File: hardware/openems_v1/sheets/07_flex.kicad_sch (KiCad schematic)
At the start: 0 parts

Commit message: feat(hw): fecha esquemático v2 — sheets 01/02/03/05/07/11 desenhadas, ERC 0
- 01_power: nova — P-FET reverse (Q1) + F1 30A + SMBJ24CA + bulk 100µF/100nF,
  star GND (PGND/SGND/AGND) via PWR_FLAG na sheet produtora, VBAT limpo para
  o resto da placa (buck/LDO ficam no TPS65381A, sheet PMIC)
- 02_ckp / 03_cmp: CKP Hall (espelho do CMP) → MCU.PA0/PA1
- 05_analog: refeita do zero a partir do pinout_v2 (13 canais ADC), mapa
  pré-v2 descartado
- 11_mcu_h562: netlist U1 corrigido (lib_id não resolvia pinos — 100 pinos
  caíam na mesma net); globals PA0/PA1/PB4 sincronizados com as sheets acima
- 07_flex: pino corrigido para PB4 (pinout_v2)
- READMEs (hardware/openems_v1, docs/hw/schematic) actualizados ao estado
  real por sheet

Passos 1-5 do roadmap do esquemático fechados; ERC isolado por sheet em 0
erros (avisos residuais são globals sem sheet destino ainda — esperado).

Co-Authored-By: Claude Sonnet 5 <noreply@anthropic.com>
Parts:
- added D1: 3V3 unidirectional, Diode_SMD:D_SOD-123, symbol Device:D_TVS
- added R1, R3: 10k, Resistor_SMD:R_0603_1608Metric, symbol Device:R
- added R2: 3k3, Resistor_SMD:R_0603_1608Metric, symbol Device:R
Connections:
- new net +5V_SENS_B: R3.1
- new net AGND: D1.2 (A2)
- new net J1.FLEX_SIG: R1.1
- new net MCU.PB4: D1.1 (A1), R1.2, R2.1, R3.2
- new net SGND: R2.2

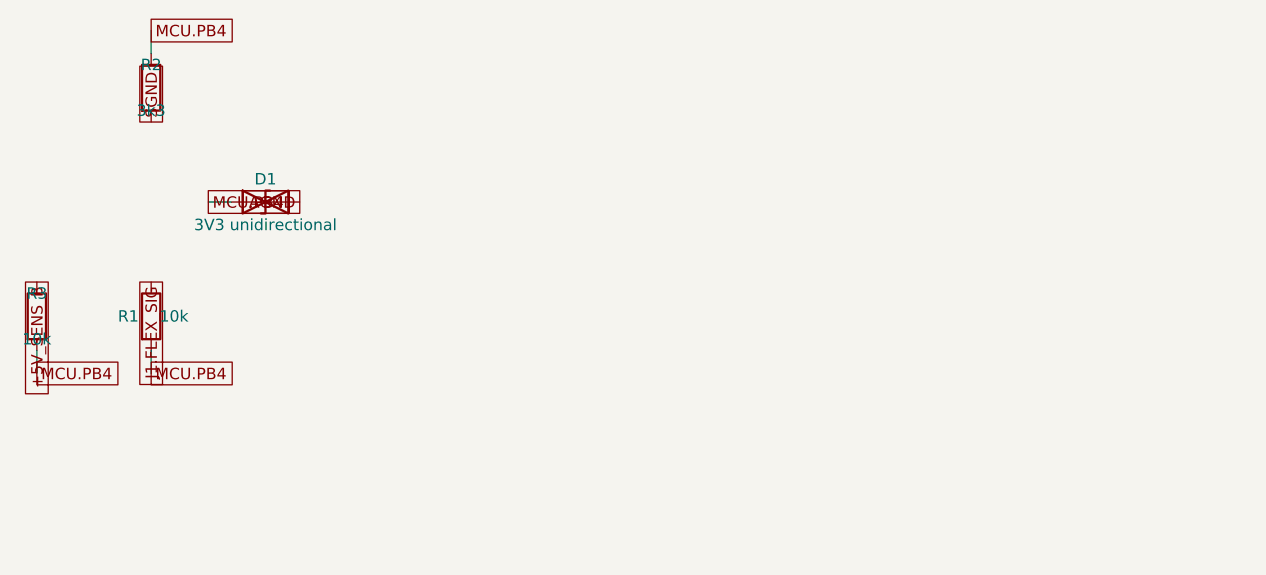
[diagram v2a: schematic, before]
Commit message: fix(hw): corrige legibilidade de 03_cmp e 07_flex — mesmo tratamento
03_cmp era clone directo do 02_ckp pré-correção (mesmo pitch de 12.7mm,
mesma sobreposição). 07_flex tinha o mesmo padrão em menor escala.
Reconstruídas com o layout validado no commit anterior — conectividade
idêntica, ERC 0 erros nas duas.

Co-Authored-By: Claude Sonnet 5 <noreply@anthropic.com>
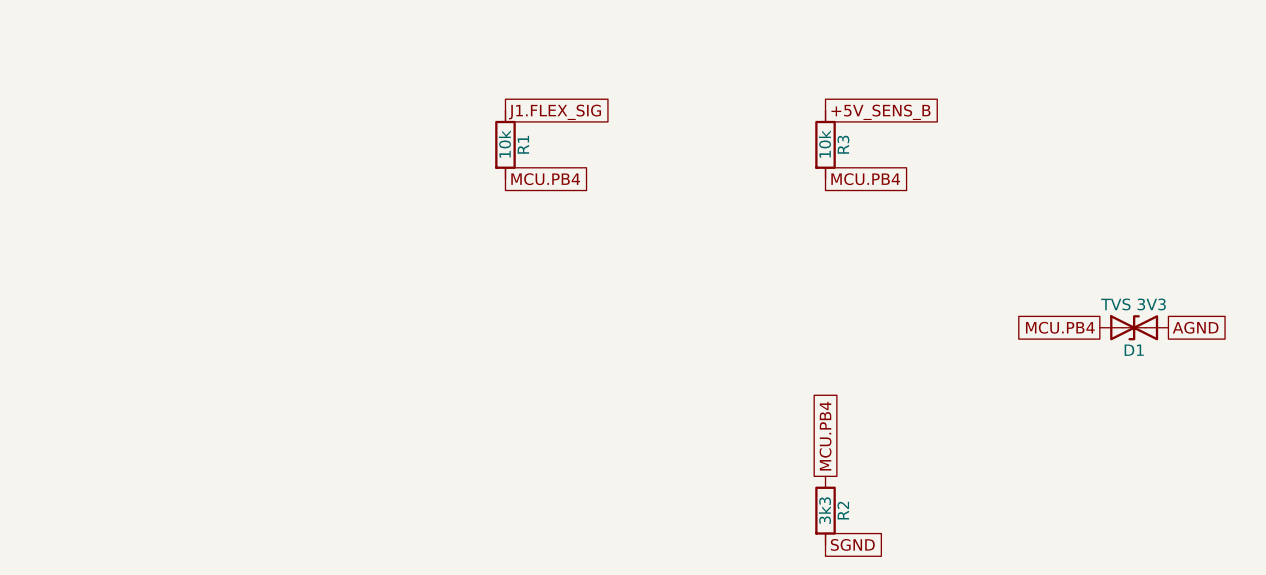
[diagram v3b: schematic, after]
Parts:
- D1: value 3V3 unidirectional -> TVS 3V3
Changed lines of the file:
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@@
 	(symbol
 		(lib_id "Device:R")
-		(at 25.4 88.9 0)
+		(at 64.77 69.85 0)
 		(unit 1)
 		(body_style 1)
@@
 		(dnp no)
 		(property "Reference" "R1"
-			(at 22.86 88.9 0)
+			(at 66.802 69.85 90)
 			(show_name no)
 			(do_not_autoplace no)
@@
 		)
 		(property "Value" "10k"
-			(at 27.94 88.9 0)
+			(at 64.77 69.85 90)
 			(show_name no)
 			(do_not_autoplace no)
@@
 		)
 		(property "Footprint" "Resistor_SMD:R_0603_1608Metric"
-			(at 23.622 88.9 90)
+			(at 62.992 69.85 90)
 			(hide yes)
 			(show_name no)
@@
 		)
 		(property "Datasheet" ""
-			(at 25.4 88.9 0)
+			(at 64.77 69.85 0)
 			(hide yes)
 			(show_name no)
@@
 		)
 		(property "Description" ""
-			(at 25.4 88.9 0)
+			(at 64.77 69.85 0)
 			(hide yes)
 			(show_name no)
@@
 					(unit 1)
 				)
-			 (path "/79296e4b-3ad2-414d-b607-9eaf9f8a1416/9a2b7e29-675b-4446-bb03-2d1d0fb3a4a2" (reference "R1") (unit 1)))
+			)
 		)
 	)
 	(symbol
 		(lib_id "Device:R")
-		(at 25.4 63.5 0)
+		(at 100.33 110.49 0)
 		(unit 1)
 		(body_style 1)
@@
 		(dnp no)
 		(property "Reference" "R2"
-			(at 25.4 60.96 0)
+			(at 102.362 110.49 90)
 			(show_name no)
 			(do_not_autoplace no)
@@
 		)
 		(property "Value" "3k3"
-			(at 25.4 66.04 0)
+			(at 100.33 110.49 90)
 			(show_name no)
 			(do_not_autoplace no)
@@
 		)
 		(property "Footprint" "Resistor_SMD:R_0603_1608Metric"
-			(at 23.622 63.5 90)
+			(at 98.552 110.49 90)
 			(hide yes)
 			(show_name no)
@@
 		)
 		(property "Datasheet" ""
-			(at 25.4 63.5 0)
+			(at 100.33 110.49 0)
 			(hide yes)
 			(show_name no)
@@
 		)
 		(property "Description" ""
-			(at 25.4 63.5 0)
+			(at 100.33 110.49 0)
 			(hide yes)
 			(show_name no)
@@
 					(unit 1)
 				)
-			 (path "/79296e4b-3ad2-414d-b607-9eaf9f8a1416/9a2b7e29-675b-4446-bb03-2d1d0fb3a4a2" (reference "R2") (unit 1)))
+			)
 		)
 	)
 	(symbol
 		(lib_id "Device:R")
-		(at 12.7 88.9 0)
+		(at 100.33 69.85 0)
 		(unit 1)
 		(body_style 1)
@@
 		(dnp no)
 		(property "Reference" "R3"
-			(at 12.7 86.36 0)
+			(at 102.362 69.85 90)
 			(show_name no)
 			(do_not_autoplace no)
@@
 		)
 		(property "Value" "10k"
-			(at 12.7 91.44 0)
+			(at 100.33 69.85 90)
 			(show_name no)
 			(do_not_autoplace no)
@@
 		)
 		(property "Footprint" "Resistor_SMD:R_0603_1608Metric"
-			(at 10.922 88.9 90)
+			(at 98.552 69.85 90)
 			(hide yes)
 			(show_name no)
@@
 		)
 		(property "Datasheet" ""
-			(at 12.7 88.9 0)
+			(at 100.33 69.85 0)
 			(hide yes)
 			(show_name no)
@@
 		)
 		(property "Description" ""
-			(at 12.7 88.9 0)
+			(at 100.33 69.85 0)
 			(hide yes)
 			(show_name no)
@@
 					(unit 1)
 				)
-			 (path "/79296e4b-3ad2-414d-b607-9eaf9f8a1416/9a2b7e29-675b-4446-bb03-2d1d0fb3a4a2" (reference "R3") (unit 1)))
+			)
 		)
 	)
 	(symbol
 		(lib_id "Device:D_TVS")
-		(at 38.1 76.2 0)
+		(at 134.62 90.17 0)
 		(unit 1)
 		(body_style 1)
@@
 		(dnp no)
 		(property "Reference" "D1"
-			(at 38.1 73.66 0)
-			(show_name no)
-			(do_not_autoplace no)
-			(effects
-				(font
-					(size 1.27 1.27)
-				)
-			)
-		)
-		(property "Value" "3V3 unidirectional"
-			(at 38.1 78.74 0)
+			(at 134.62 92.71 0)
+			(show_name no)
+			(do_not_autoplace no)
+			(effects
+				(font
+					(size 1.27 1.27)
+				)
+			)
+		)
+		(property "Value" "TVS 3V3"
+			(at 134.62 87.63 0)
 			(show_name no)
 			(do_not_autoplace no)
@@
 		)
 		(property "Footprint" "Diode_SMD:D_SOD-123"
-			(at 38.1 76.2 0)
+			(at 134.62 90.17 0)
 			(hide yes)
 			(show_name no)
@@
 		)
 		(property "Datasheet" ""
-			(at 38.1 76.2 0)
+			(at 134.62 90.17 0)
 			(hide yes)
 			(show_name no)
@@
 		)
 		(property "Description" ""
-			(at 38.1 76.2 0)
+			(at 134.62 90.17 0)
 			(hide yes)
 			(show_name no)
@@
 					(unit 1)
 				)
-			 (path "/79296e4b-3ad2-414d-b607-9eaf9f8a1416/9a2b7e29-675b-4446-bb03-2d1d0fb3a4a2" (reference "D1") (unit 1)))
+			)
 		)
 	)
 	(global_label "J1.FLEX_SIG"
-		(at 25.4 85.09 270)
+		(at 64.77 66.03999999999999 0)
+		(effects
+			(font
+				(size 1.27 1.27)
+			)
+			(justify left)
+		)
+	)
+	(global_label "MCU.PB4"
+		(at 64.77 73.66 0)
+		(effects
+			(font
+				(size 1.27 1.27)
+			)
+			(justify left)
+		)
+	)
+	(global_label "+5V_SENS_B"
+		(at 100.33 66.03999999999999 0)
+		(effects
+			(font
+				(size 1.27 1.27)
+			)
+			(justify left)
+		)
+	)
+	(global_label "MCU.PB4"
+		(at 100.33 73.66 0)
+		(effects
+			(font
+				(size 1.27 1.27)
+			)
+			(justify left)
+		)
+	)
+	(global_label "MCU.PB4"
+		(at 100.33 106.67999999999999 90)
+		(effects
+			(font
+				(size 1.27 1.27)
+			)
+			(justify left)
+		)
+	)
+	(global_label "SGND"
+		(at 100.33 114.3 0)
+		(effects
+			(font
+				(size 1.27 1.27)
+			)
+			(justify left)
+		)
+	)
+	(global_label "MCU.PB4"
+		(at 130.81 90.17 180)
 		(effects
 			(font
@@
 		)
 	)
-	(global_label "SGND"
-		(at 25.4 67.31 90)
-		(effects
-			(font
-				(size 1.27 1.27)
-			)
-			(justify left)
-		)
-	)
-	(global_label "+5V_SENS_B"
-		(at 12.7 85.09 270)
-		(effects
-			(font
-				(size 1.27 1.27)
-			)
-			(justify right)
-		)
-	)
 	(global_label "AGND"
-		(at 41.910000000000004 76.2 180)
-		(effects
-			(font
-				(size 1.27 1.27)
-			)
-			(justify right)
-		)
-	)
-	(wire
-		(pts
-			(xy 25.4 92.71000000000001) (xy 25.4 95.25)
-		)
-		(stroke
-			(width 0)
-			(type default)
-		)
-	)
-	(wire
-		(pts
-			(xy 25.4 59.69) (xy 25.4 57.15)
-		)
-		(stroke
-			(width 0)
-			(type default)
-		)
-	)
-	(wire
-		(pts
-			(xy 12.7 92.71000000000001) (xy 12.7 95.25)
-		)
-		(stroke
-			(width 0)
-			(type default)
-		)
-	)
-	(wire
-		(pts
-			(xy 34.29 76.2) (xy 31.75 76.2)
-		)
-		(stroke
-			(width 0)
-			(type default)
-		)
-	)
-	(global_label "MCU.PB4"
-		(at 25.4 95.25 0)
-		(effects
-			(font
-				(size 1.27 1.27)
-			)
-			(justify left)
-		)
-	)
-	(global_label "MCU.PB4"
-		(at 25.4 57.15 0)
-		(effects
-			(font
-				(size 1.27 1.27)
-			)
-			(justify left)
-		)
-	)
-	(global_label "MCU.PB4"
-		(at 12.7 95.25 0)
-		(effects
-			(font
-				(size 1.27 1.27)
-			)
-			(justify left)
-		)
-	)
-	(global_label "MCU.PB4"
-		(at 31.75 76.2 0)
-		(effects
-			(font
+		(at 138.43 90.17 0)
+		(effects
+			(font
